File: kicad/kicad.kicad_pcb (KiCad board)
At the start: 2 copper layers, 68.8 x 53.6 mm, 9 parts, among them U1 74HC595, U2 74HC595, U3 AT28C256_40PIN_ZIF

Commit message: KiCad: Updated PCB.
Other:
- board text added: "EEPROM Pin 1"
- board text added: "Erik van Zijst, 2019 erik.van.zijst@gmail.com https://github.com/erikvanzijst/eeprom"
- board text added: "For use with 256K AT28C256 only"
- board text added: "v01"
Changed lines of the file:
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@@
   (general
     (thickness 1.6)
-    (drawings 10)
+    (drawings 19)
     (tracks 338)
     (zones 0)
@@
       (net 64 "Net-(XA1-PadMISO)"))
   )
+  (gr_text "For use with 256K AT28C256 only" (at 153.162 66.294) (layer F.SilkS)
+    (effects (font (size 1 1) (thickness 0.15)))
+  )
+  (gr_text "Erik van Zijst, 2019\nerik.van.zijst@gmail.com\nhttps://github.com/erikvanzijst/eeprom" (at 191.008 105.41) (layer B.SilkS)
+    (effects (font (size 1 1) (thickness 0.15)) (justify left mirror))
+  )
+  (gr_text "EEPROM Pin 1" (at 185.166 66.294) (layer F.SilkS)
+    (effects (font (size 1 1) (thickness 0.15)))
+  )
+  (gr_line (start 191.77 67.056) (end 191.008 67.564) (layer F.SilkS) (width 0.12))
+  (gr_line (start 191.77 67.056) (end 191.008 66.548) (layer F.SilkS) (width 0.12))
+  (gr_line (start 191.77 67.056) (end 179.832 67.056) (layer F.SilkS) (width 0.12))
+  (gr_line (start 191.77 65.786) (end 191.77 68.202) (layer F.SilkS) (width 0.12))
+  (gr_text v01 (at 132.842 61.976) (layer B.Cu)
+    (effects (font (size 1.5 1.5) (thickness 0.3)) (justify mirror))
+  )
+  (gr_text v01 (at 133.096 61.976) (layer F.Cu)
+    (effects (font (size 1.5 1.5) (thickness 0.3)))
+  )
   (gr_text "EEPROM Programmer Shield for\nArduino UNO R3" (at 144.653 105.537) (layer F.SilkS)

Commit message: KiCad: Updated PCB.
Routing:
- net VCC: track 88.2 -> 84.0 mm
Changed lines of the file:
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@@
     (thickness 1.6)
     (drawings 19)
-    (tracks 338)
+    (tracks 335)
     (zones 0)
     (modules 9)
@@
     (visible_elements FFFFFF7F)
     (pcbplotparams
-      (layerselection 0x010fc_ffffffff)
-      (usegerberextensions false)
+      (layerselection 0x010f0_ffffffff)
+      (usegerberextensions true)
       (usegerberattributes false)
       (usegerberadvancedattributes false)
@@
       (psa4output false)
       (plotreference true)
-      (plotvalue true)
+      (plotvalue false)
       (plotinvisibletext false)
       (padsonsilk false)
@@
       (outputformat 1)
       (mirror false)
-      (drillshape 1)
+      (drillshape 0)
       (scaleselection 1)
-      (outputdirectory ""))
+      (outputdirectory "gerbers/"))
   )
   (net 0 "")
@@
   (segment (start 160.909 98.425) (end 160.909 96.788) (width 0.762) (layer F.Cu) (net 2))
   (via (at 160.909 98.425) (size 0.6858) (drill 0.3302) (layers F.Cu B.Cu) (net 2))
-  (segment (start 159.385 99.949) (end 160.909 98.425) (width 0.762) (layer B.Cu) (net 2))
-  (segment (start 160.02 107.696) (end 159.385 107.061) (width 0.762) (layer B.Cu) (net 2))
-  (segment (start 159.385 107.061) (end 159.385 99.949) (width 0.762) (layer B.Cu) (net 2))
-  (segment (start 165.084 107.696) (end 160.02 107.696) (width 0.762) (layer B.Cu) (net 2))
-  (segment (start 168.461001 111.073001) (end 165.084 107.696) (width 0.762) (layer B.Cu) (net 2))
   (segment (start 178.449 98.411) (end 178.449 100.635) (width 0.762) (layer F.Cu) (net 2))
   (via (at 178.449 98.411) (size 0.6858) (drill 0.3302) (layers F.Cu B.Cu) (net 2))
@@
   (segment (start 171.838002 107.696) (end 186.69 107.696) (width 0.762) (layer B.Cu) (net 2))
   (segment (start 168.461001 111.073001) (end 171.838002 107.696) (width 0.762) (layer B.Cu) (net 2))
+  (segment (start 168.461001 105.977001) (end 160.909 98.425) (width 0.762) (layer B.Cu) (net 2))
+  (segment (start 168.461001 111.073001) (end 168.461001 105.977001) (width 0.762) (layer B.Cu) (net 2))
   (segment (start 140.718792 97.028) (end 146.05 97.028) (width 0.1778) (layer F.Cu) (net 3))
   (segment (start 139.446 97.028) (end 140.718792 97.028) (width 0.1778) (layer F.Cu) (net 3))

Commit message: Added silkscreen logo to PCB.
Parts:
- added G***: LOGO, EEPROM:erik_600dpi, B.Cu at (193.5, 96.3)

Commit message: KiCad: Added 400dpi logo.
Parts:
- removed the G*** at (193.5, 96.3)
- added G***: LOGO, EEPROM:erik_400dpi_small, B.Cu at (193.4, 96.6)

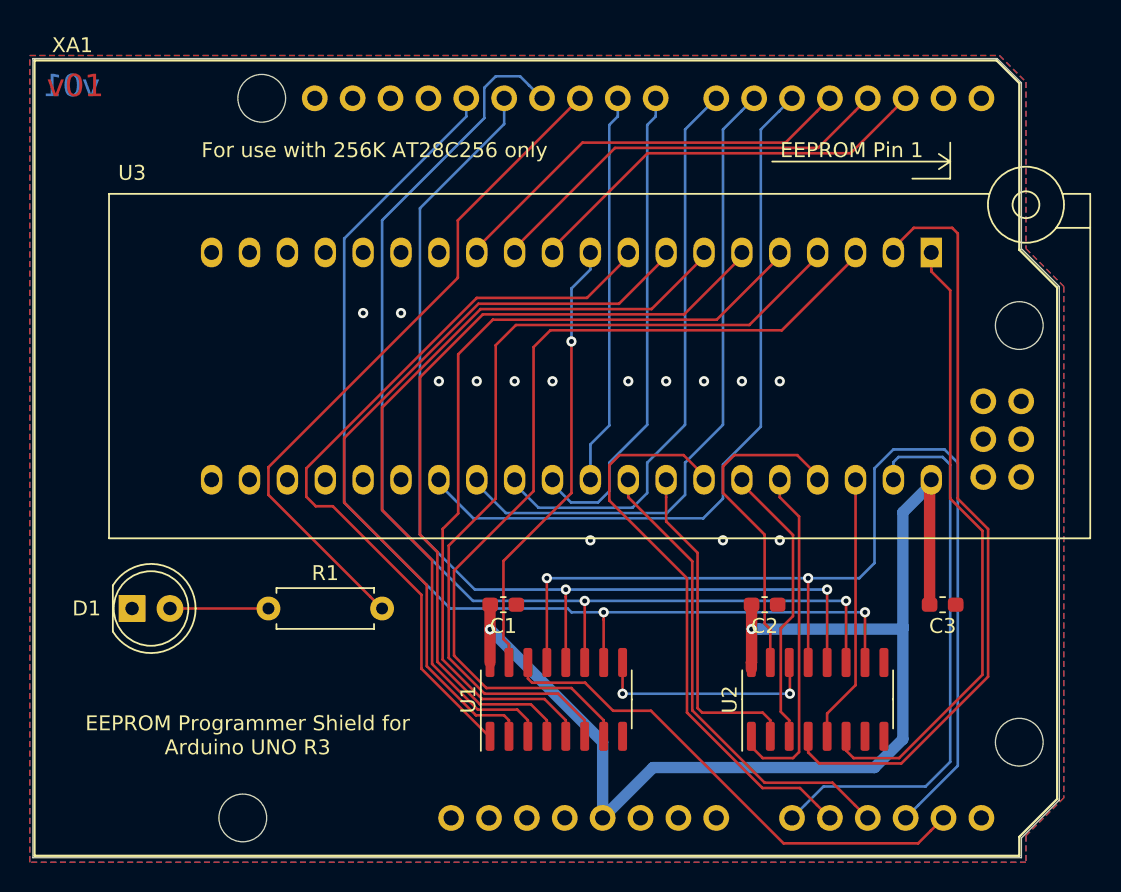
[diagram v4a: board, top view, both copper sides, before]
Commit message: KiCad: Updated OSH Park permalink and moved cap to backside.
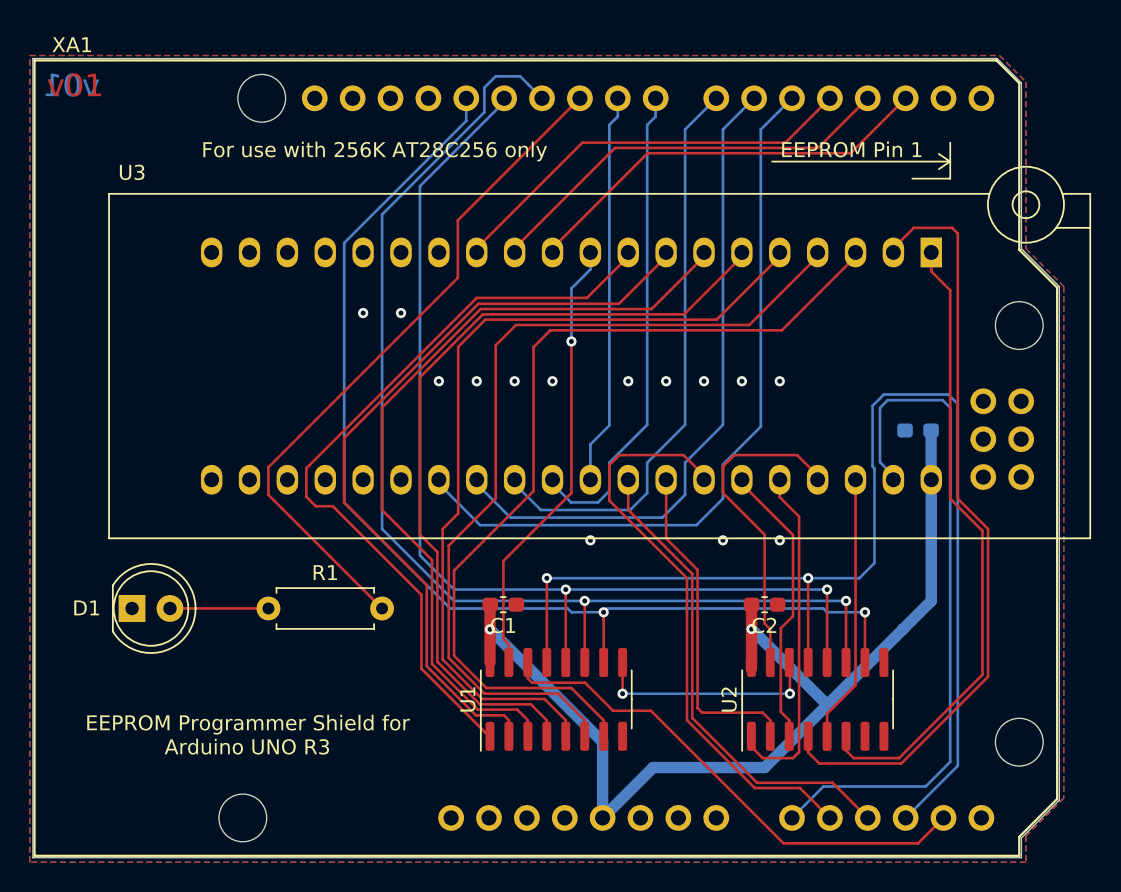
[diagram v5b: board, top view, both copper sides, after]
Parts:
- C3: moved to B.Cu
- moved C3 11.8 mm to (189.6, 85.1), turned to 0 degrees
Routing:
- net VCC: track 84.0 -> 71.5 mm
- net /~WE: track 37.4 -> 46.2 mm
- net /~SOE: track 71.8 -> 79.8 mm
- net /RCLK: track 70.2 -> 71.0 mm
- net /SCLK: track 77.9 -> 78.6 mm
